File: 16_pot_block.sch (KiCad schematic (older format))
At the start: 21 parts, among them U3 CD74HC4067M

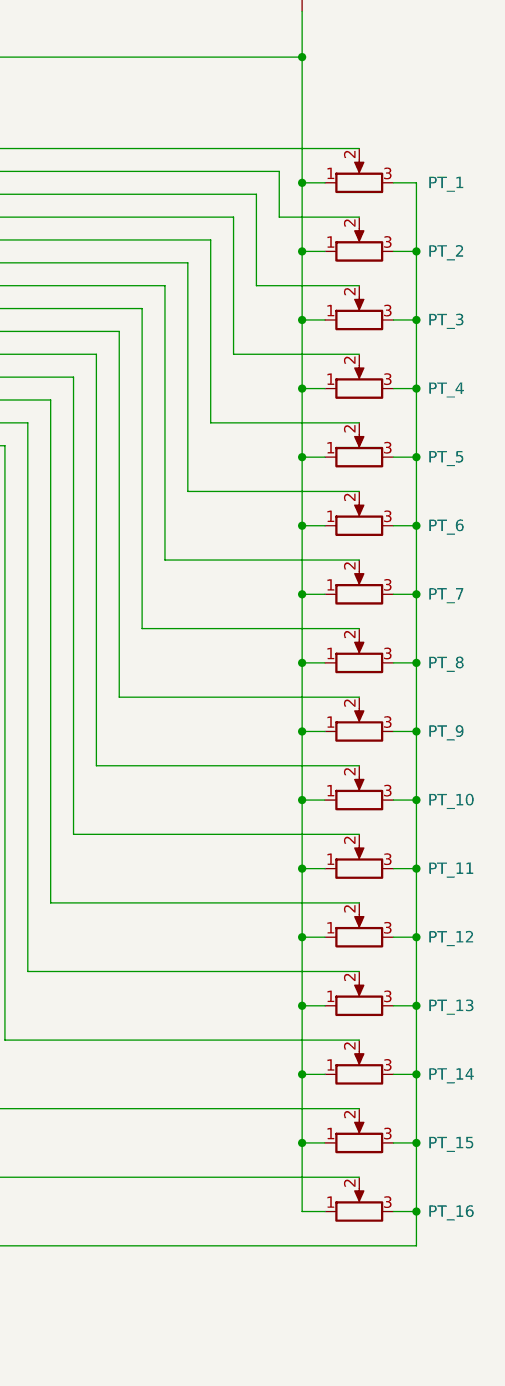
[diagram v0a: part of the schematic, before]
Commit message: Updated Schematic and changed rotary pots
Better button symbol and flipped all rotary pots in the schematic so they've connected the right way round.

Changed the rotary pot footprints so the graphics match the ones I'm using.
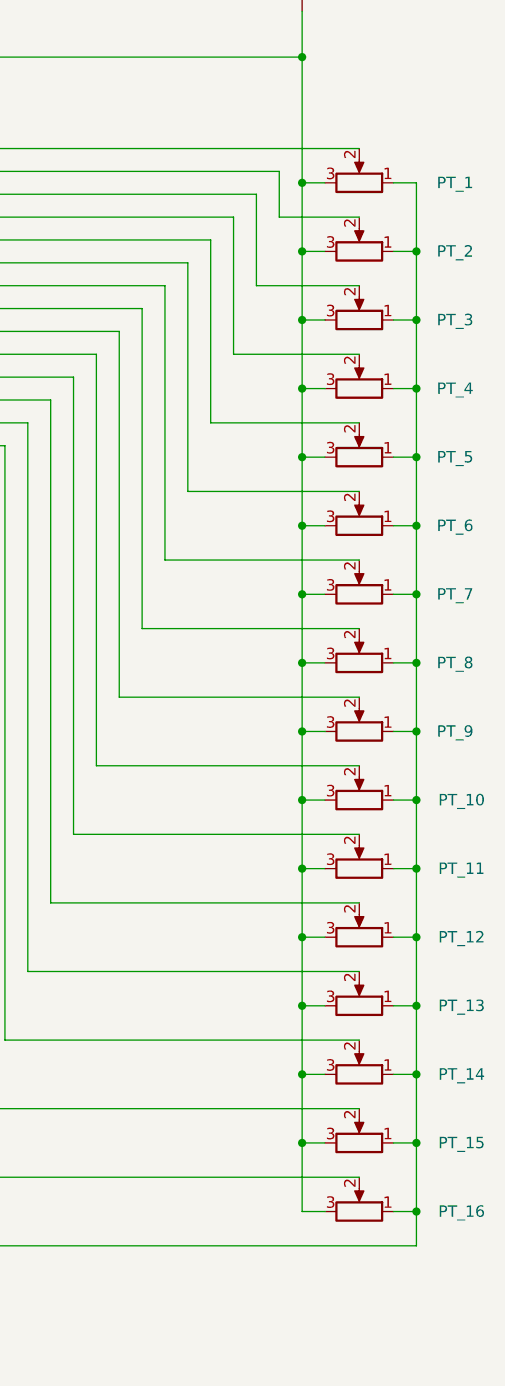
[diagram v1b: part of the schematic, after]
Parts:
- PT_1, PT_10, PT_11, PT_12, PT_13, PT_14, PT_15, PT_16, PT_2, PT_3, PT_4, PT_5, PT_6, PT_7, PT_8, PT_9: footprint cunabulapress-footprints:Potentiometer_Alps_RK09K_Single_Vertical_Edit -> cunabulapress-footprints:Potentiometer_Alps_RK09D1130X
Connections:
- net +5V: now also PT_1.3, PT_10.3, PT_11.3, PT_12.3, PT_13.3, PT_14.3, PT_15.3, PT_16.3, PT_2.3, PT_3.3, PT_4.3, PT_5.3, PT_6.3, PT_7.3, PT_8.3, PT_9.3; no longer PT_1.1, PT_10.1, PT_11.1, PT_12.1, PT_13.1, PT_14.1, PT_15.1, PT_16.1, PT_2.1, PT_3.1, PT_4.1, PT_5.1, PT_6.1, PT_7.1, PT_8.1, PT_9.1
- net GND: now also PT_1.1, PT_10.1, PT_11.1, PT_12.1, PT_13.1, PT_14.1, PT_15.1, PT_16.1, PT_2.1, PT_3.1, PT_4.1, PT_5.1, PT_6.1, PT_7.1, PT_8.1, PT_9.1; no longer PT_1.3, PT_10.3, PT_11.3, PT_12.3, PT_13.3, PT_14.3, PT_15.3, PT_16.3, PT_2.3, PT_3.3, PT_4.3, PT_5.3, PT_6.3, PT_7.3, PT_8.3, PT_9.3
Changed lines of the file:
@@
 EESchema Schematic File Version 4
 LIBS:cp_midi_control_surface_002-cache
-EELAYER 30 0
+EELAYER 26 0
 EELAYER END
 $Descr A4 11693 8268
@@
 U 1 1 5C26C20B
 P 5050 1700
-F 0 "PT_1" V 5050 1400 50  0000 R CNN
+F 0 "PT_1" V 5050 2200 50  0000 R CNN
 F 1 "10k" H 4980 1655 50  0001 R CNN
-F 2 "cunabulapress-footprints:Potentiometer_Alps_RK09K_Single_Vertical_Edit" H 5050 1700 50  0001 C CNN
+F 2 "cunabulapress-footprints:Potentiometer_Alps_RK09D1130X" H 5050 1700 50  0001 C CNN
 F 3 "~" H 5050 1700 50  0001 C CNN
 	1    5050 1700
-	0    -1   -1   0
+	0    1    -1   0
 $EndComp
 $Comp
@@
 U 1 1 5C26C26F
 P 5050 2000
-F 0 "PT_2" V 5050 1700 50  0000 R CNN
+F 0 "PT_2" V 5050 2500 50  0000 R CNN
 F 1 "10k" H 4980 1955 50  0001 R CNN
-F 2 "cunabulapress-footprints:Potentiometer_Alps_RK09K_Single_Vertical_Edit" H 5050 2000 50  0001 C CNN
+F 2 "cunabulapress-footprints:Potentiometer_Alps_RK09D1130X" H 5050 2000 50  0001 C CNN
 F 3 "~" H 5050 2000 50  0001 C CNN
 	1    5050 2000
-	0    -1   -1   0
+	0    1    -1   0
 $EndComp
 $Comp
@@
 U 1 1 5C26C8F7
 P 5050 2300
-F 0 "PT_3" V 5050 2000 50  0000 R CNN
+F 0 "PT_3" V 5050 2800 50  0000 R CNN
 F 1 "10k" H 4980 2255 50  0001 R CNN
-F 2 "cunabulapress-footprints:Potentiometer_Alps_RK09K_Single_Vertical_Edit" H 5050 2300 50  0001 C CNN
+F 2 "cunabulapress-footprints:Potentiometer_Alps_RK09D1130X" H 5050 2300 50  0001 C CNN
 F 3 "~" H 5050 2300 50  0001 C CNN
 	1    5050 2300
-	0    -1   -1   0
+	0    1    -1   0
 $EndComp
 $Comp
@@
 U 1 1 5C26CB54
 P 5050 2600
-F 0 "PT_4" V 5050 2300 50  0000 R CNN
+F 0 "PT_4" V 5050 3100 50  0000 R CNN
 F 1 "10k" H 4980 2555 50  0001 R CNN
-F 2 "cunabulapress-footprints:Potentiometer_Alps_RK09K_Single_Vertical_Edit" H 5050 2600 50  0001 C CNN
+F 2 "cunabulapress-footprints:Potentiometer_Alps_RK09D1130X" H 5050 2600 50  0001 C CNN
 F 3 "~" H 5050 2600 50  0001 C CNN
 	1    5050 2600
-	0    -1   -1   0
+	0    1    -1   0
 $EndComp
 $Comp
@@
 U 1 1 5C26CB7C
 P 5050 2900
-F 0 "PT_5" V 5050 2600 50  0000 R CNN
+F 0 "PT_5" V 5050 3400 50  0000 R CNN
 F 1 "10k" V 5050 2900 50  0001 C CNN
-F 2 "cunabulapress-footprints:Potentiometer_Alps_RK09K_Single_Vertical_Edit" H 5050 2900 50  0001 C CNN
+F 2 "cunabulapress-footprints:Potentiometer_Alps_RK09D1130X" H 5050 2900 50  0001 C CNN
 F 3 "~" H 5050 2900 50  0001 C CNN
 	1    5050 2900
-	0    -1   -1   0
+	0    1    -1   0
 $EndComp
 $Comp
@@
 U 1 1 5C26CBA6
 P 5050 3200
-F 0 "PT_6" V 5050 2900 50  0000 R CNN
+F 0 "PT_6" V 5050 3700 50  0000 R CNN
 F 1 "10k" H 4980 3155 50  0001 R CNN
-F 2 "cunabulapress-footprints:Potentiometer_Alps_RK09K_Single_Vertical_Edit" H 5050 3200 50  0001 C CNN
+F 2 "cunabulapress-footprints:Potentiometer_Alps_RK09D1130X" H 5050 3200 50  0001 C CNN
 F 3 "~" H 5050 3200 50  0001 C CNN
 	1    5050 3200
-	0    -1   -1   0
+	0    1    -1   0
 $EndComp
 $Comp
@@
 U 1 1 5C26CBD2
 P 5050 3500
-F 0 "PT_7" V 5050 3200 50  0000 R CNN
+F 0 "PT_7" V 5050 4000 50  0000 R CNN
 F 1 "10k" H 4980 3455 50  0001 R CNN
-F 2 "cunabulapress-footprints:Potentiometer_Alps_RK09K_Single_Vertical_Edit" H 5050 3500 50  0001 C CNN
+F 2 "cunabulapress-footprints:Potentiometer_Alps_RK09D1130X" H 5050 3500 50  0001 C CNN
 F 3 "~" H 5050 3500 50  0001 C CNN
 	1    5050 3500
-	0    -1   -1   0
+	0    1    -1   0
 $EndComp
 $Comp
@@
 U 1 1 5C26CDC5
 P 5050 3800
-F 0 "PT_8" V 5050 3500 50  0000 R CNN
+F 0 "PT_8" V 5050 4300 50  0000 R CNN
 F 1 "10k" H 4980 3755 50  0001 R CNN
-F 2 "cunabulapress-footprints:Potentiometer_Alps_RK09K_Single_Vertical_Edit" H 5050 3800 50  0001 C CNN
+F 2 "cunabulapress-footprints:Potentiometer_Alps_RK09D1130X" H 5050 3800 50  0001 C CNN
 F 3 "~" H 5050 3800 50  0001 C CNN
 	1    5050 3800
-	0    -1   -1   0
+	0    1    -1   0
 $EndComp
 $Comp
@@
 U 1 1 5C26D143
 P 5050 4100
-F 0 "PT_9" V 5050 3800 50  0000 R CNN
+F 0 "PT_9" V 5050 4600 50  0000 R CNN
 F 1 "10k" H 4980 4055 50  0001 R CNN
-F 2 "cunabulapress-footprints:Potentiometer_Alps_RK09K_Single_Vertical_Edit" H 5050 4100 50  0001 C CNN
+F 2 "cunabulapress-footprints:Potentiometer_Alps_RK09D1130X" H 5050 4100 50  0001 C CNN
 F 3 "~" H 5050 4100 50  0001 C CNN
 	1    5050 4100
-	0    -1   -1   0
+	0    1    -1   0
 $EndComp
 $Comp
@@
 U 1 1 5C26D193
 P 5050 4400
-F 0 "PT_10" V 5050 4100 50  0000 R CNN
+F 0 "PT_10" V 5050 4950 50  0000 R CNN
 F 1 "10k" H 4980 4355 50  0001 R CNN
-F 2 "cunabulapress-footprints:Potentiometer_Alps_RK09K_Single_Vertical_Edit" H 5050 4400 50  0001 C CNN
+F 2 "cunabulapress-footprints:Potentiometer_Alps_RK09D1130X" H 5050 4400 50  0001 C CNN
 F 3 "~" H 5050 4400 50  0001 C CNN
 	1    5050 4400
-	0    -1   -1   0
+	0    1    -1   0
 $EndComp
 $Comp
@@
 U 1 1 5C26D1C9
 P 5050 4700
-F 0 "PT_11" V 5050 4400 50  0000 R CNN
+F 0 "PT_11" V 5050 5250 50  0000 R CNN
 F 1 "10k" H 4980 4655 50  0001 R CNN
-F 2 "cunabulapress-footprints:Potentiometer_Alps_RK09K_Single_Vertical_Edit" H 5050 4700 50  0001 C CNN
+F 2 "cunabulapress-footprints:Potentiometer_Alps_RK09D1130X" H 5050 4700 50  0001 C CNN
 F 3 "~" H 5050 4700 50  0001 C CNN
 	1    5050 4700
-	0    -1   -1   0
+	0    1    -1   0
 $EndComp
 $Comp
@@
 U 1 1 5C26D201
 P 5050 5000
-F 0 "PT_12" V 5050 4700 50  0000 R CNN
+F 0 "PT_12" V 5050 5550 50  0000 R CNN
 F 1 "10k" H 4980 4955 50  0001 R CNN
-F 2 "cunabulapress-footprints:Potentiometer_Alps_RK09K_Single_Vertical_Edit" H 5050 5000 50  0001 C CNN
+F 2 "cunabulapress-footprints:Potentiometer_Alps_RK09D1130X" H 5050 5000 50  0001 C CNN
 F 3 "~" H 5050 5000 50  0001 C CNN
 	1    5050 5000
-	0    -1   -1   0
+	0    1    -1   0
 $EndComp
 $Comp
@@
 U 1 1 5C26D23B
 P 5050 5300
-F 0 "PT_13" V 5050 5000 50  0000 R CNN
+F 0 "PT_13" V 5050 5850 50  0000 R CNN
 F 1 "10k" H 4980 5255 50  0001 R CNN
-F 2 "cunabulapress-footprints:Potentiometer_Alps_RK09K_Single_Vertical_Edit" H 5050 5300 50  0001 C CNN
+F 2 "cunabulapress-footprints:Potentiometer_Alps_RK09D1130X" H 5050 5300 50  0001 C CNN
 F 3 "~" H 5050 5300 50  0001 C CNN
 	1    5050 5300
-	0    -1   -1   0
+	0    1    -1   0
 $EndComp
 $Comp
@@
 U 1 1 5C26D27D
 P 5050 5600
-F 0 "PT_14" V 5050 5300 50  0000 R CNN
+F 0 "PT_14" V 5050 6150 50  0000 R CNN
 F 1 "10k" H 4980 5555 50  0001 R CNN
-F 2 "cunabulapress-footprints:Potentiometer_Alps_RK09K_Single_Vertical_Edit" H 5050 5600 50  0001 C CNN
+F 2 "cunabulapress-footprints:Potentiometer_Alps_RK09D1130X" H 5050 5600 50  0001 C CNN
 F 3 "~" H 5050 5600 50  0001 C CNN
 	1    5050 5600
-	0    -1   -1   0
+	0    1    -1   0
 $EndComp
 $Comp
@@
 U 1 1 5C26D38D
 P 5050 5900
-F 0 "PT_15" V 5050 5600 50  0000 R CNN
+F 0 "PT_15" V 5050 6450 50  0000 R CNN
 F 1 "10k" H 4980 5855 50  0001 R CNN
-F 2 "cunabulapress-footprints:Potentiometer_Alps_RK09K_Single_Vertical_Edit" H 5050 5900 50  0001 C CNN
+F 2 "cunabulapress-footprints:Potentiometer_Alps_RK09D1130X" H 5050 5900 50  0001 C CNN
 F 3 "~" H 5050 5900 50  0001 C CNN
 	1    5050 5900
-	0    -1   -1   0
+	0    1    -1   0
 $EndComp
 $Comp
@@
 U 1 1 5C26D3C9
 P 5050 6200
-F 0 "PT_16" V 5050 5900 50  0000 R CNN
+F 0 "PT_16" V 5050 6750 50  0000 R CNN
 F 1 "10k" H 4980 6155 50  0001 R CNN
-F 2 "cunabulapress-footprints:Potentiometer_Alps_RK09K_Single_Vertical_Edit" H 5050 6200 50  0001 C CNN
+F 2 "cunabulapress-footprints:Potentiometer_Alps_RK09D1130X" H 5050 6200 50  0001 C CNN
 F 3 "~" H 5050 6200 50  0001 C CNN
 	1    5050 6200
-	0    -1   -1   0
+	0    1    -1   0
 $EndComp
 Wire Wire Line
